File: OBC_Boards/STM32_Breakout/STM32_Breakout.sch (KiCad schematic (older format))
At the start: 48 parts, among them U1 STM32L4R5ZIT6P, U2 STM32F446RETx, U3 STM32L4A6ZGT6P, U4 IR4301

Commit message: Add footprints for the power monitor circuit
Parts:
- removed C17: 2.2uF, Capacitor_SMD:C_0603_1608Metric_Pad1.08x0.95mm_HandSolder, symbol Device:C_Small
- removed CurSense1: 20mO, symbol Device:R
- removed D3: RED, LED_SMD:LED_0603_1608Metric_Pad1.05x0.95mm_HandSolder, symbol Device:LED_Small
- removed R7: 10k, RESC1607X60N, symbol STM32_Breakout-rescue:R0603-OBC_Libary
- removed U1: STM32L4R5ZIT6P, QFP50P2200X2200X160-144N, symbol STM32_Breakout-rescue:STM32L4R5ZIT6P-STM32L4R5ZIT6P
- removed U2: STM32F446RETx, Package_QFP:LQFP-64_10x10mm_P0.5mm, symbol MCU_ST_STM32F4:STM32F446RETx
- removed U4: IR4301, Package_DFN_QFN:Infineon_PQFN-22-15-4EP_6x5mm_P0.65mm, symbol Amplifier_Audio:IR4301
- added R6: 20m, RESC1607X60N, symbol STM32_Breakout-rescue:R0603-OBC_Libary
- MAX4372F1: renamed from MAX4372F; footprint Max4372FESA+:SOIC127P600X175-8N -> STM32_Breakout:SOIC127P600X175-8N; symbol MAX4372FESA+:MAX4372FESA+ -> STM32_Breakout-rescue:MAX4372FESA+-MAX4372FESA+
- renumbered C1 to C18, C2 to C19
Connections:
- net labels removed: HSE_In, HSE_Out
- wire segments 111 -> 89
- no-connect marks 35 -> 2

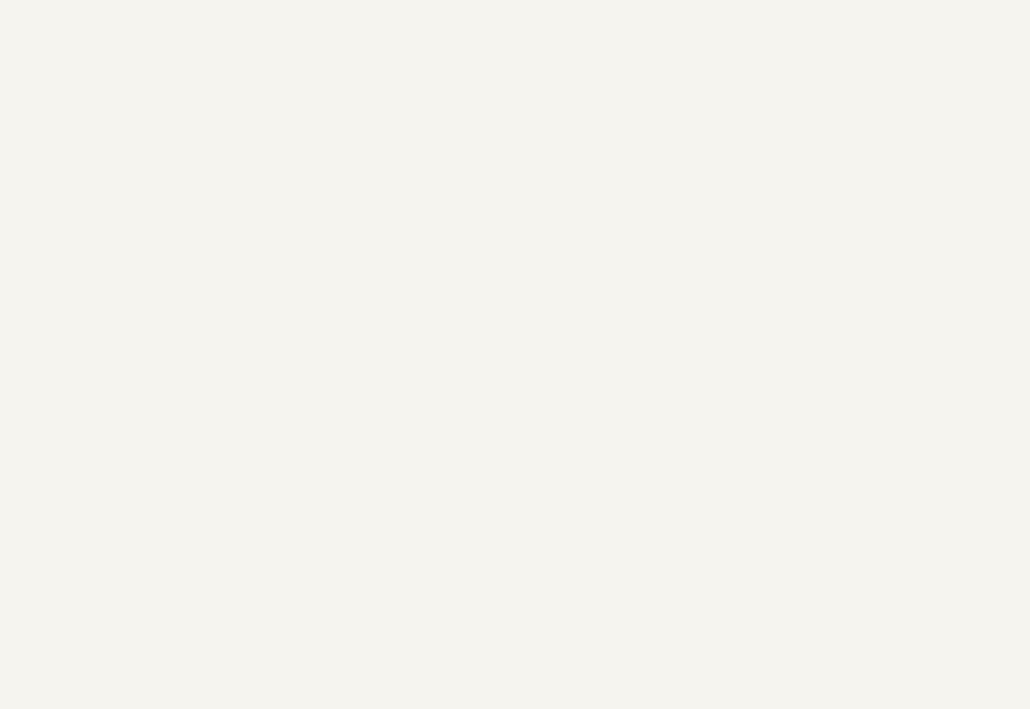
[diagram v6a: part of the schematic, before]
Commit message: MRAM symbol added
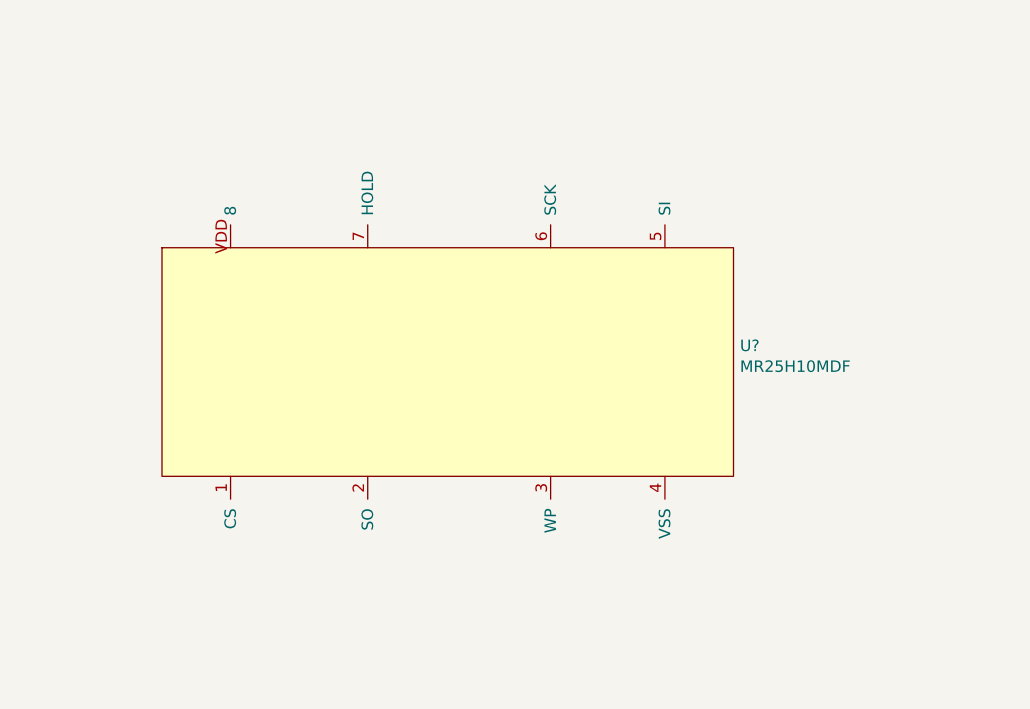
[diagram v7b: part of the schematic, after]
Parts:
- added U?: MR25H10MDF, Footprint:SON65P300X300X95-8N, symbol MRAM_Symbol:MR25H10MDF
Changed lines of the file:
@@
 EESchema Schematic File Version 4
-LIBS:STM32_Breakout-cache
 EELAYER 30 0
 EELAYER END
@@
 	3250 1550 3450 1550
 Connection ~ 3450 1550
+$Comp
+L MRAM_Symbol:MR25H10MDF U?
+U 1 1 61A91C31
+P 12650 10000
+F 0 "U?" H 13878 10571 50  0000 L CNN
+F 1 "MR25H10MDF" H 13878 10480 50  0000 L CNN
+F 2 "Footprint:SON65P300X300X95-8N" H 12650 9200 50  0001 C CNN
+F 3 "" H 12650 9200 50  0001 C CNN
+	1    12650 10000
+	1    0    0    -1
+$EndComp
 $EndSCHEMATC

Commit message: Fix symbol error on MRAM
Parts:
- U?: symbol MRAM_Symbol:MR25H10MDF -> STM32_Breakout-rescue:MR25H10MDF-MRAM_Symbol
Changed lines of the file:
@@
 EESchema Schematic File Version 4
+LIBS:STM32_Breakout-cache
 EELAYER 30 0
 EELAYER END
@@
 Connection ~ 3450 1550
 $Comp
-L MRAM_Symbol:MR25H10MDF U?
+L STM32_Breakout-rescue:MR25H10MDF-MRAM_Symbol U?
 U 1 1 61A91C31
 P 12650 10000
